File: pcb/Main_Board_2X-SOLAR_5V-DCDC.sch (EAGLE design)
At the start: 71 parts, among them CN5 USBA_FEMALE, IC1 MCP73871, IC2 MCP73871, T2 MMUN2133LT1G, U3 TPS61090RSAR, X1 Solar input, X2 5V output

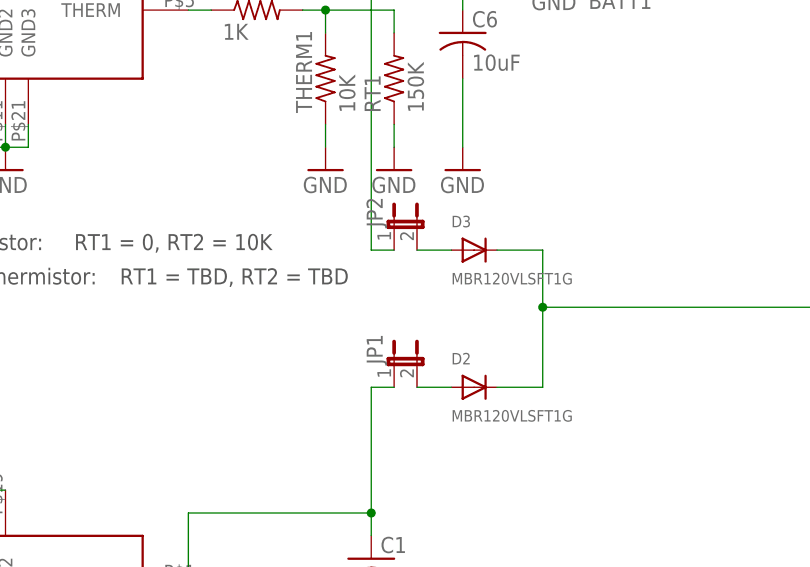
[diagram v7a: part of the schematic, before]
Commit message: OSH revision. No jumpers, compressed layout
Shrank the layout of the board to a smaller size and removed the jumpers for easier assembly
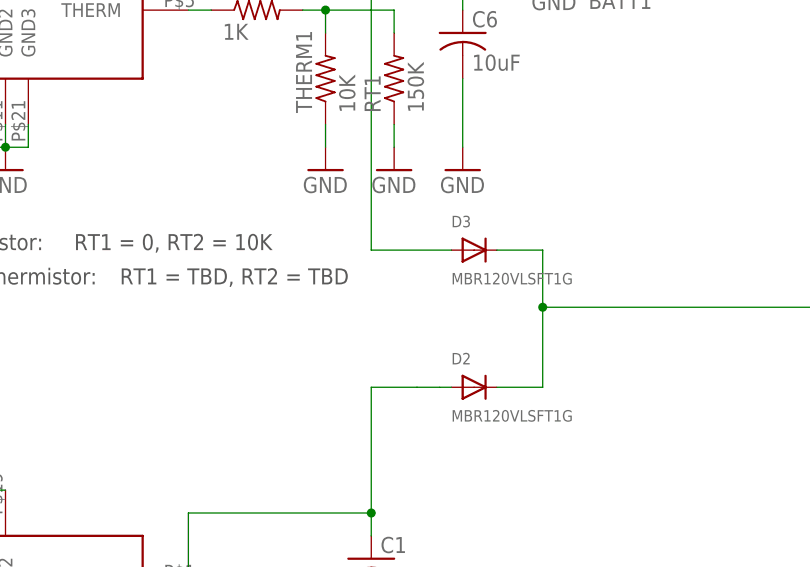
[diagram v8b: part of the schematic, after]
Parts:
- removed JP1, JP2: (no value), jumper:JP1E
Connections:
- removed net DIODE_PROT: D2.A, JP1.2
- removed net DIODE_PROT_1: D3.A, JP2.2
- net VOUT: now also D2.A; no longer JP1.1
- net VOUT1: now also D3.A; no longer JP2.1
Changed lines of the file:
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@@
 <?xml version="1.0" encoding="utf-8"?>
 <!DOCTYPE eagle SYSTEM "eagle.dtd">
-<eagle version="8.2.1">
+<eagle version="8.2.2">
 <drawing>
 <settings>
@@
 <part name="D2" library="microbuilder" deviceset="DIODE" device="SOD-123" value="MBR120VLSFT1G"/>
 <part name="D3" library="microbuilder" deviceset="DIODE" device="SOD-123" value="MBR120VLSFT1G"/>
-<part name="JP1" library="jumper" library_urn="urn:adsk.eagle:library:252" deviceset="JP1E" device=""/>
-<part name="JP2" library="jumper" library_urn="urn:adsk.eagle:library:252" deviceset="JP1E" device=""/>
 </parts>
 <sheets>
@@
 <instance part="D2" gate="G$1" x="191.77" y="86.36"/>
 <instance part="D3" gate="G$1" x="191.77" y="101.6"/>
-<instance part="JP1" gate="A" x="182.88" y="88.9"/>
-<instance part="JP2" gate="A" x="182.88" y="104.14"/>
 </instances>
 <busses>
@@
 <pinref part="C5" gate="G$1" pin="1"/>
 <wire x1="180.34" y1="158.75" x2="180.34" y2="101.6" width="0.1524" layer="91"/>
-<wire x1="180.34" y1="101.6" x2="182.88" y2="101.6" width="0.1524" layer="91"/>
 <junction x="180.34" y="158.75"/>
-<pinref part="JP2" gate="A" pin="1"/>
+<pinref part="D3" gate="G$1" pin="A"/>
+<wire x1="180.34" y1="101.6" x2="189.23" y2="101.6" width="0.1524" layer="91"/>
 </segment>
 </net>
@@
 <pinref part="IC1" gate="G$1" pin="OUT2"/>
 <wire x1="180.34" y1="72.39" x2="180.34" y2="86.36" width="0.1524" layer="91"/>
-<wire x1="180.34" y1="86.36" x2="182.88" y2="86.36" width="0.1524" layer="91"/>
 <junction x="180.34" y="72.39"/>
-<pinref part="JP1" gate="A" pin="1"/>
-</segment>
-</net>
-<net name="DIODE_PROT_1" class="0">
-<segment>
-<pinref part="D3" gate="G$1" pin="A"/>
-<pinref part="JP2" gate="A" pin="2"/>
-<wire x1="185.42" y1="101.6" x2="189.23" y2="101.6" width="0.1524" layer="91"/>
-</segment>
-</net>
-<net name="DIODE_PROT" class="0">
-<segment>
 <pinref part="D2" gate="G$1" pin="A"/>
-<pinref part="JP1" gate="A" pin="2"/>
-<wire x1="185.42" y1="86.36" x2="189.23" y2="86.36" width="0.1524" layer="91"/>
+<wire x1="185.42" y1="86.36" x2="187.96" y2="86.36" width="0.1524" layer="91"/>
+<wire x1="187.96" y1="86.36" x2="189.23" y2="86.36" width="0.1524" layer="91"/>
+<wire x1="180.34" y1="86.36" x2="185.42" y2="86.36" width="0.1524" layer="91"/>
 </segment>
 </net>
@@
 </schematic>
 </drawing>
-<compatibility>
-<note version="8.2" severity="warning">
-Since Version 8.2, Eagle supports online libraries. The ids
-of those online libraries will not be understood (or retained)
-with this version.
-</note>
-</compatibility>
 </eagle>
